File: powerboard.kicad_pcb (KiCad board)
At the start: 2 copper layers, 81.3 x 63.5 mm, 28 parts, among them J1 B03B, J2 EMER_SW, J3 EMER_SW, Q1 TJ60S04M3L, U1 PQQ10W-Q24-S5-S, U2 TLP222A

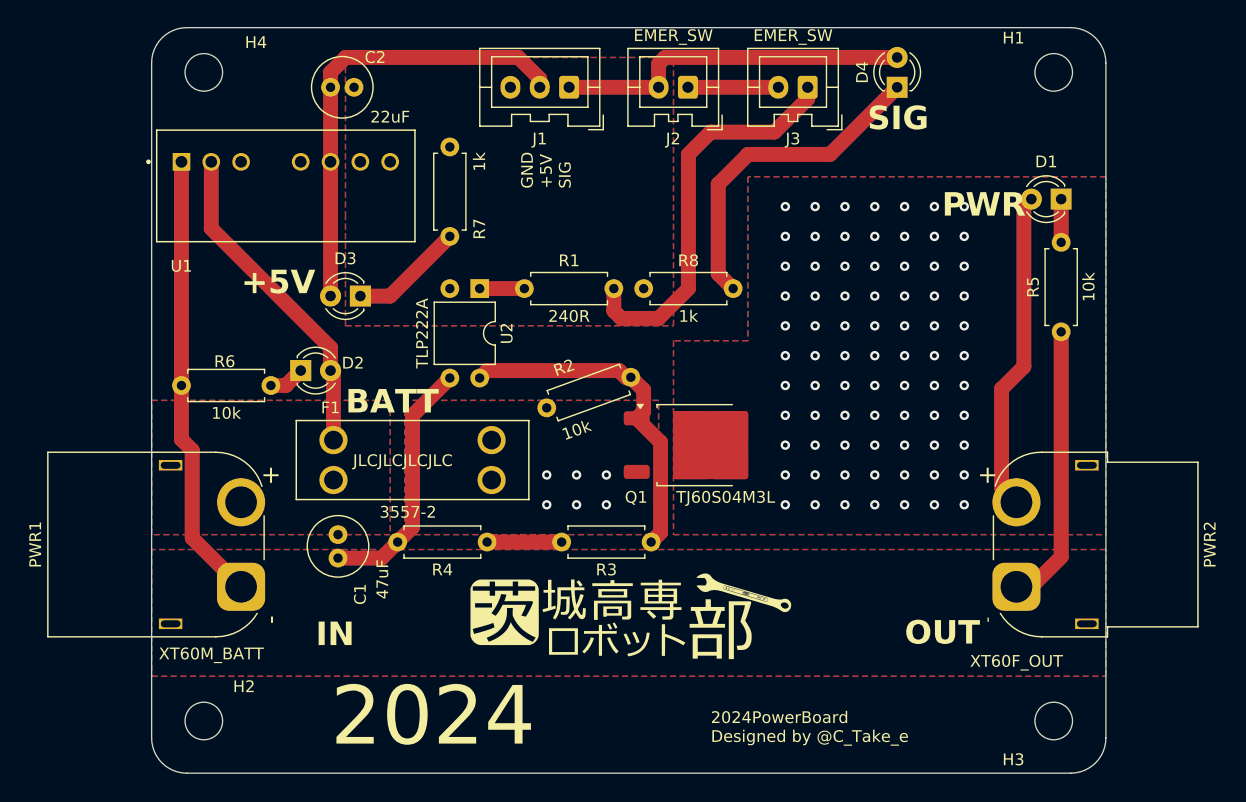
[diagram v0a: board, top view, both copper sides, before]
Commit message: クソデカ24Vシルク追加
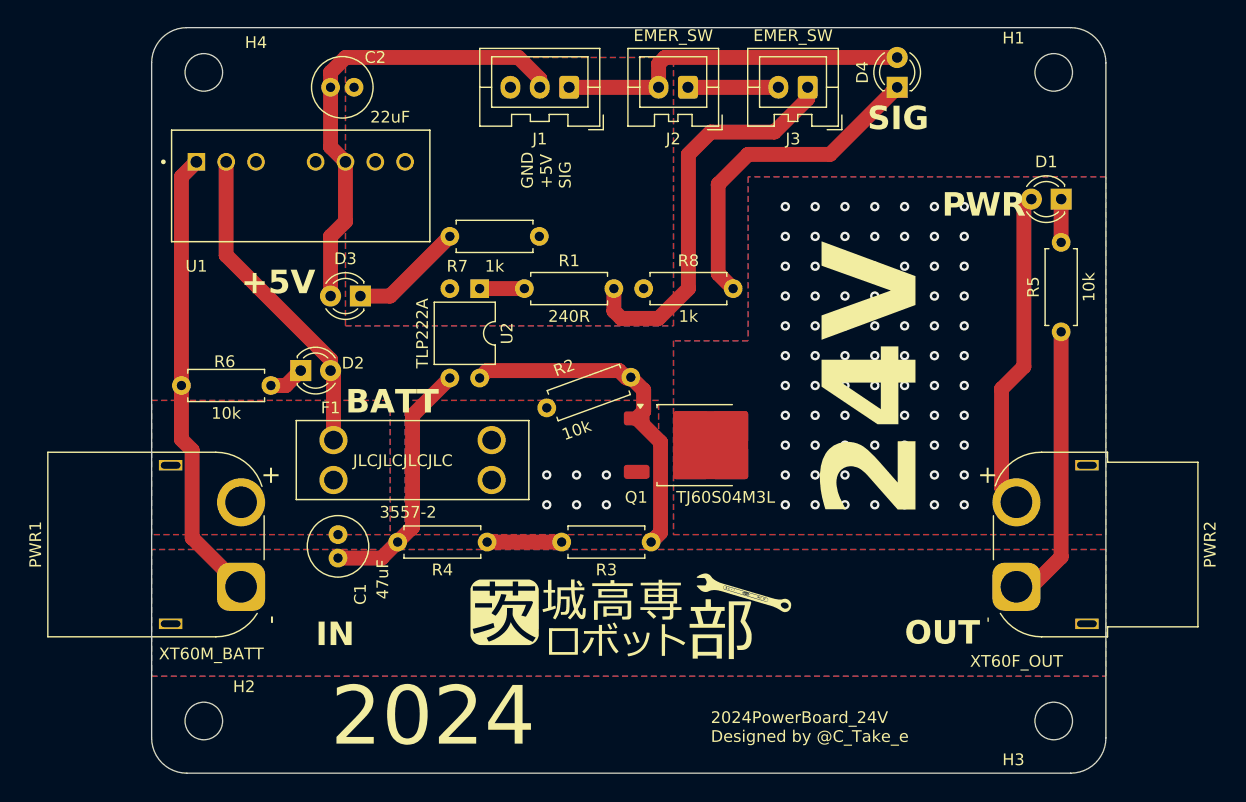
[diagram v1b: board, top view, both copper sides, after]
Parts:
- moved U1 1.27 mm to (128.3, 97.3)
- turned R7 to 0 degrees
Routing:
- net +5V: track 38.9 -> 39.9 mm
- net GNDPWR: track 84.4 -> 85.0 mm
- net BATT: track 28.0 -> 27.5 mm
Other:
- board text added: "2024PowerBoard_24V Designed by @C_Take_e"
- board text added: "24V"
- board text removed: "2024PowerBoard Designed by @C_Take_e"

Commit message: ツェナーで定電圧チャレンジ
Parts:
- removed R3, R4: 10k, Resistor_THT:R_Axial_DIN0207_L6.3mm_D2.5mm_P7.62mm_Horizontal
- added D5: BZX55C9V1, Diode_THT:D_DO-35_SOD27_P10.16mm_Horizontal, F.Cu at (146.7, 115.3)
- R2: value 10k -> 1k8
- moved R2 15.3 mm to (163.6, 111.0), turned to -160 degrees
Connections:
- R2 pad 1: VDD -> Net-(D5-A)
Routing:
- net FET_G: track 28.9 -> 17.1 mm
- net Net-(D5-A): track 0.00 -> 8.37 mm
- net Net-(R3-Pad2): track 6.35 -> 0.00 mm

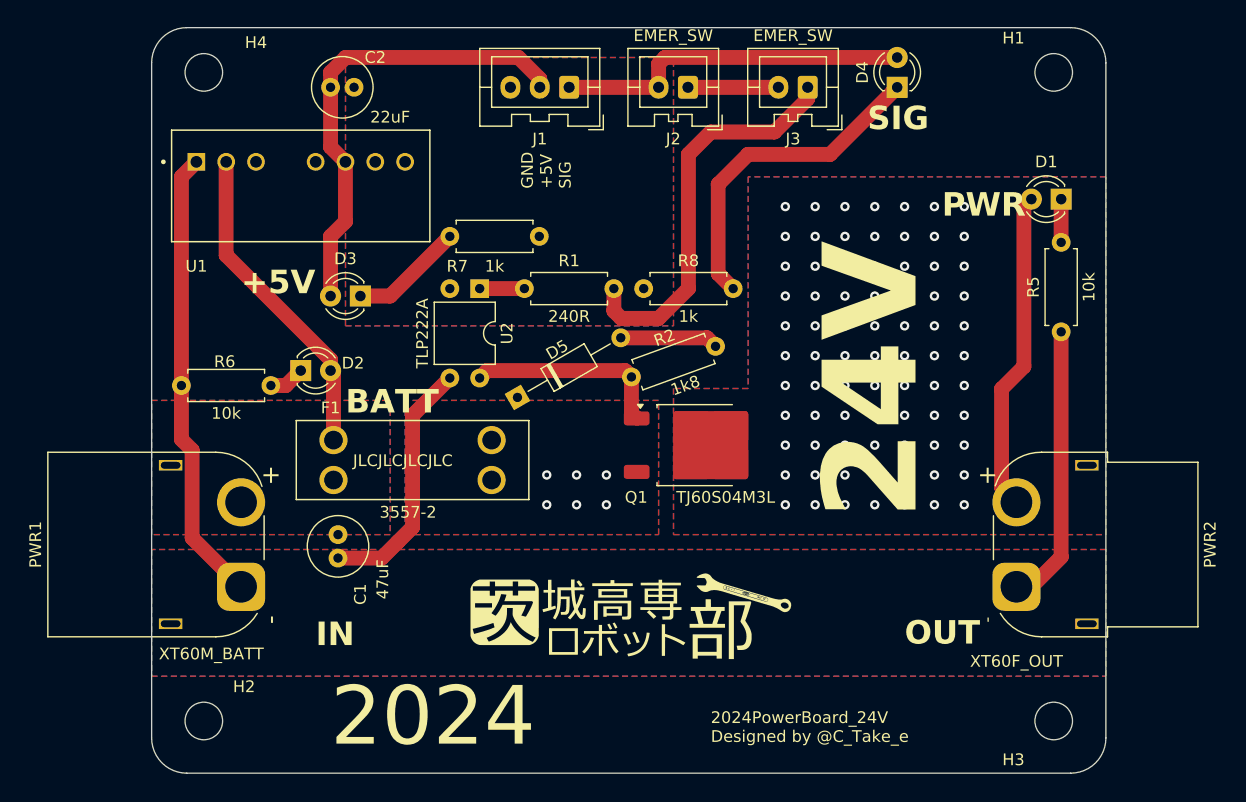
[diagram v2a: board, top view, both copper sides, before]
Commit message: ツェナー回り修正、DCDC入力コンデンサ位置変更
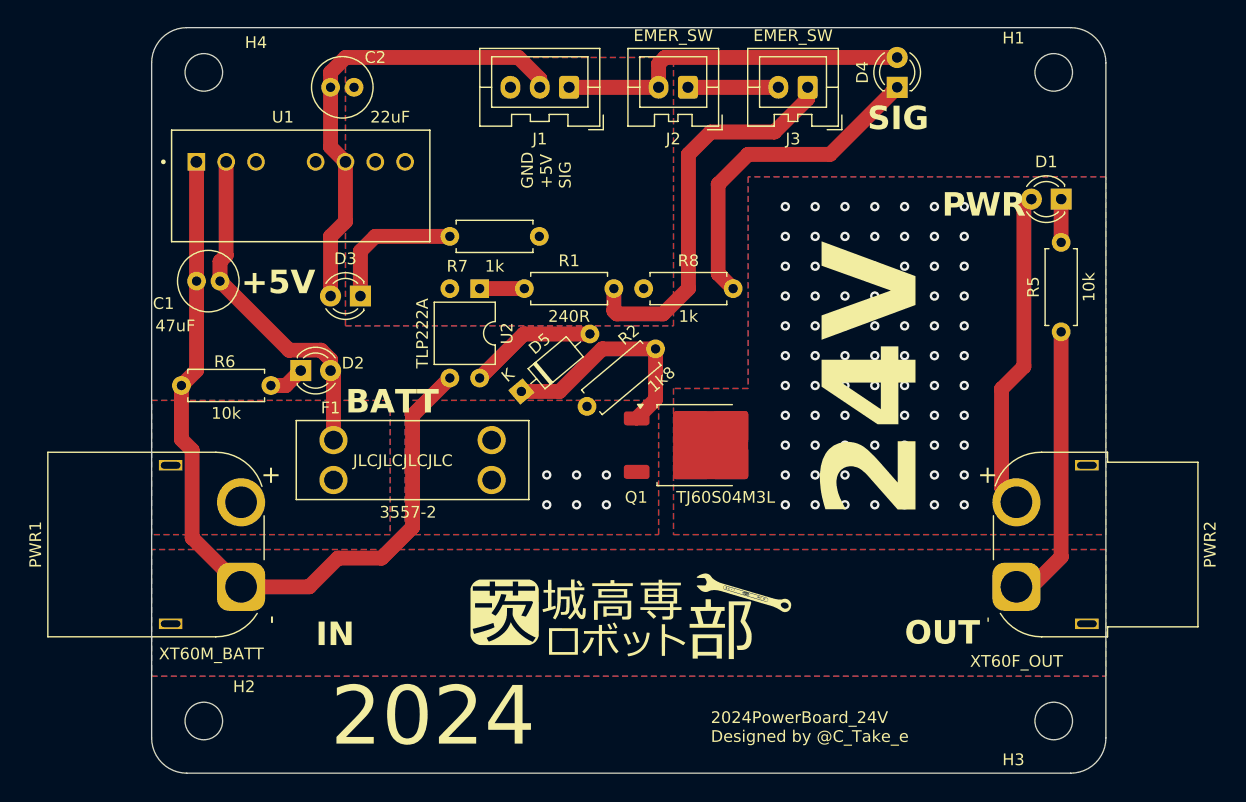
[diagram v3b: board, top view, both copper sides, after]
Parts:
- D5: footprint Diode_THT:D_DO-35_SOD27_P10.16mm_Horizontal -> Diode_THT:D_DO-35_SOD27_P7.62mm_Horizontal
- moved C1 23.8 mm to (121.4, 105.4), turned to 180 degrees
- moved R2 12.1 mm to (152.7, 116.1), turned to 40 degrees
- moved D5 0.61 mm to (147.1, 114.8), turned to 40 degrees
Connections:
- D5 pad 1: VDD -> Net-(D5-K)
- D5 pad 2: Net-(D5-A) -> FET_G
- Q1 pad 1: FET_G -> Net-(D5-K)
- R2 pad 1: Net-(D5-A) -> VDD
- R2 pad 2: FET_G -> Net-(D5-K)
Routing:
- net Net-(D5-K): track 0.00 -> 19.5 mm
- net GNDPWR: track 85.0 -> 93.6 mm
- net Net-(D5-A): track 8.37 -> 0.00 mm
- net FET_G: track 17.1 -> 10.9 mm
- net Net-(D3-K): track 9.72 -> 12.0 mm
- net BATT: track 27.5 -> 29.5 mm

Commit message: コンデンサ追加、フップリ修正
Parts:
- added C3: C_Polarized, Capacitor_THT:CP_Radial_D16.0mm_P7.50mm, F.Cu at (177.0, 124.6)
- C1: footprint Capacitor_THT:C_Radial_D5.0mm_H11.0mm_P2.00mm -> Capacitor_THT:CP_Radial_D6.3mm_P2.50mm
- C2: footprint Capacitor_THT:C_Radial_D5.0mm_H11.0mm_P2.00mm -> Capacitor_THT:CP_Radial_D5.0mm_P2.00mm
- moved C1 0.76 mm to (121.4, 106.2)
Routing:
- net VOUT: vias 77 -> 76

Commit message: あれこれ
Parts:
- H1, H2, H3, H4: footprint MountingHole:MountingHole_3.2mm_M3 -> MountingHole:MountingHole_3.2mm_M3_Pad_Via
- moved H1 0.64 mm to (192.4, 88.3)
- moved H4 0.64 mm to (120.0, 88.3)
